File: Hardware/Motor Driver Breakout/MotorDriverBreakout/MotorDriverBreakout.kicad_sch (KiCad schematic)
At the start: 49 parts, among them U1 DRV8234RTER, U2 DRV8234RTER, U2 MCP4725A1T-E/CH, U3 MCP4725A1T-E/CH, U5 TPSM33625RDNR, U7 TPSM33625RDNR, U8 TPSM33625RDNR

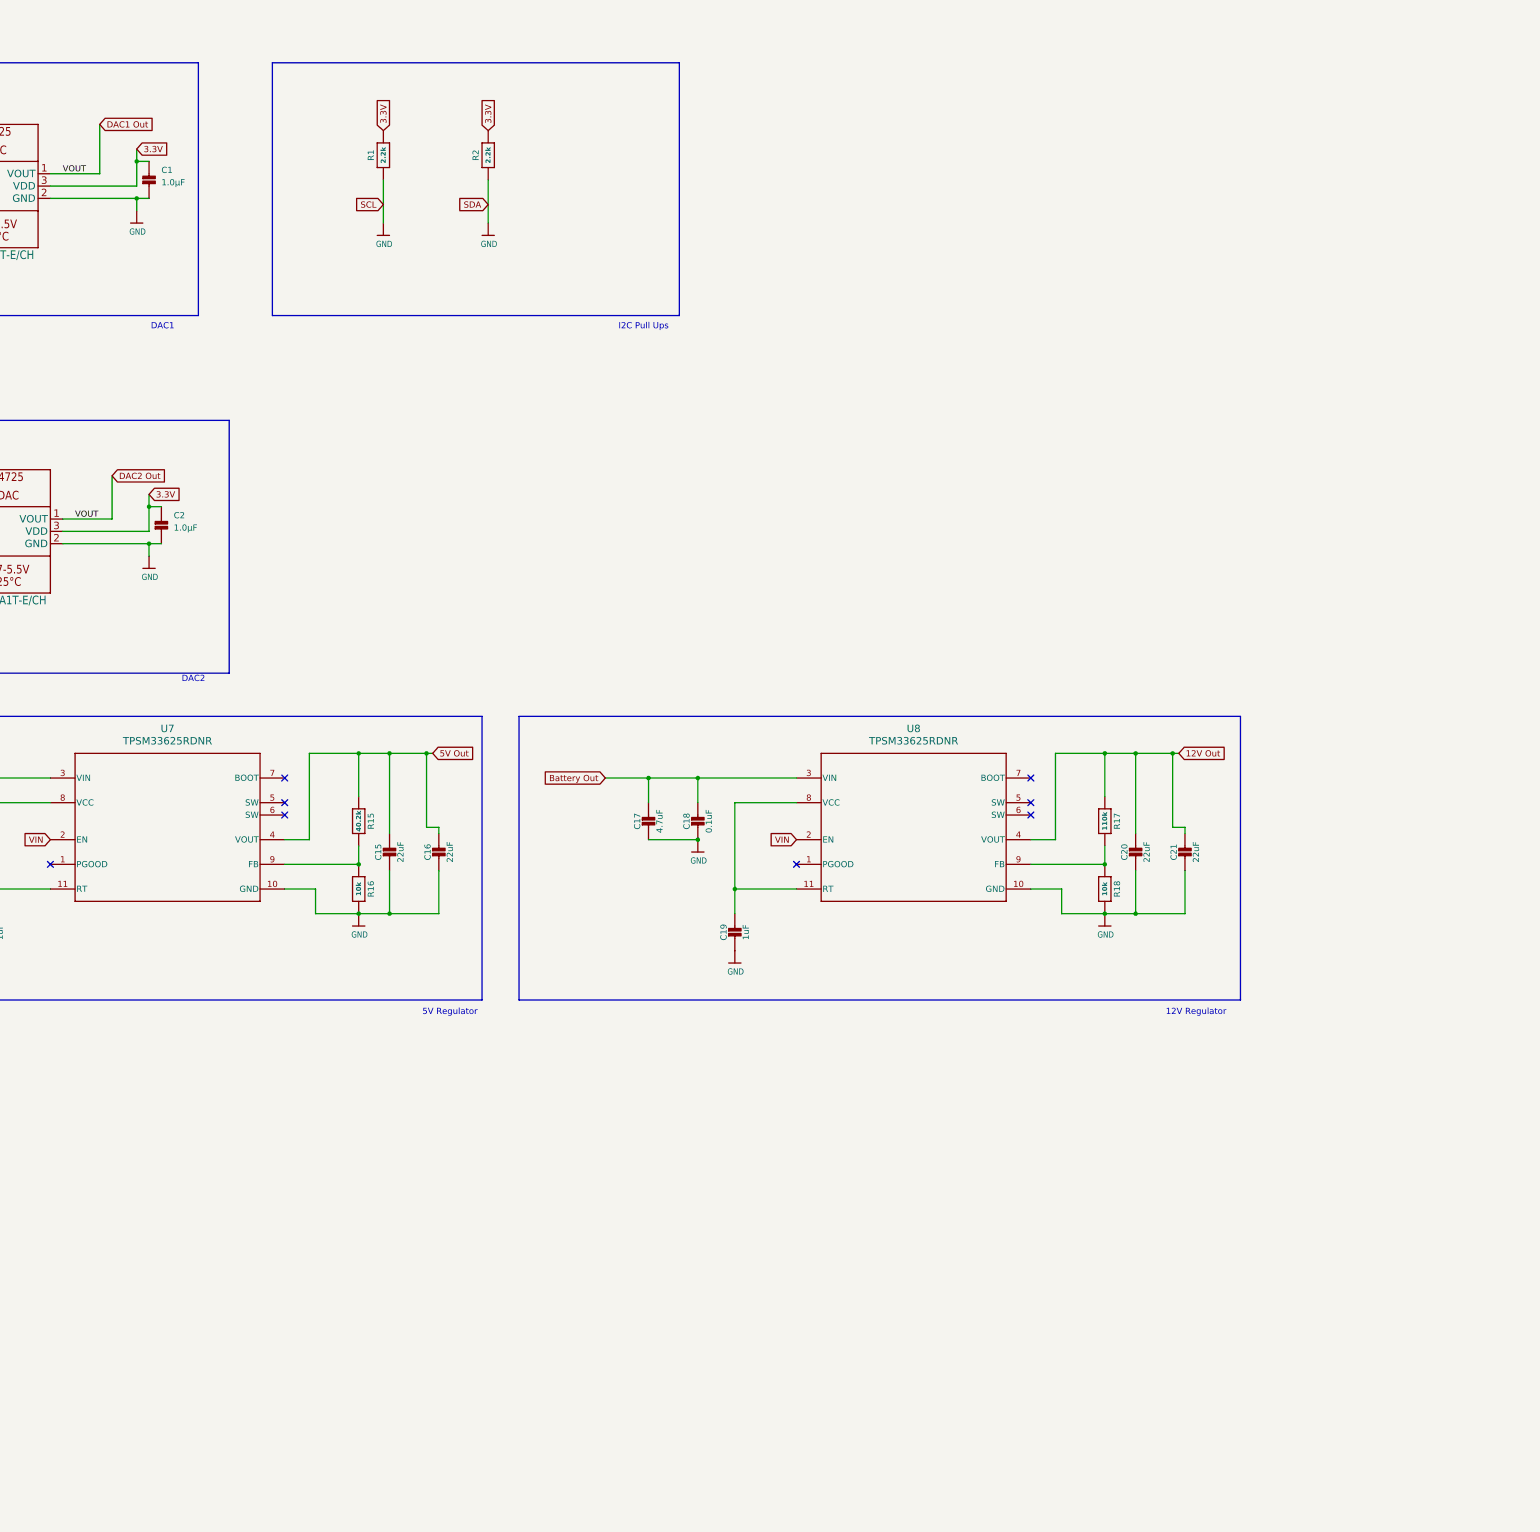
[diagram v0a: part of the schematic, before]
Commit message: Added another driver
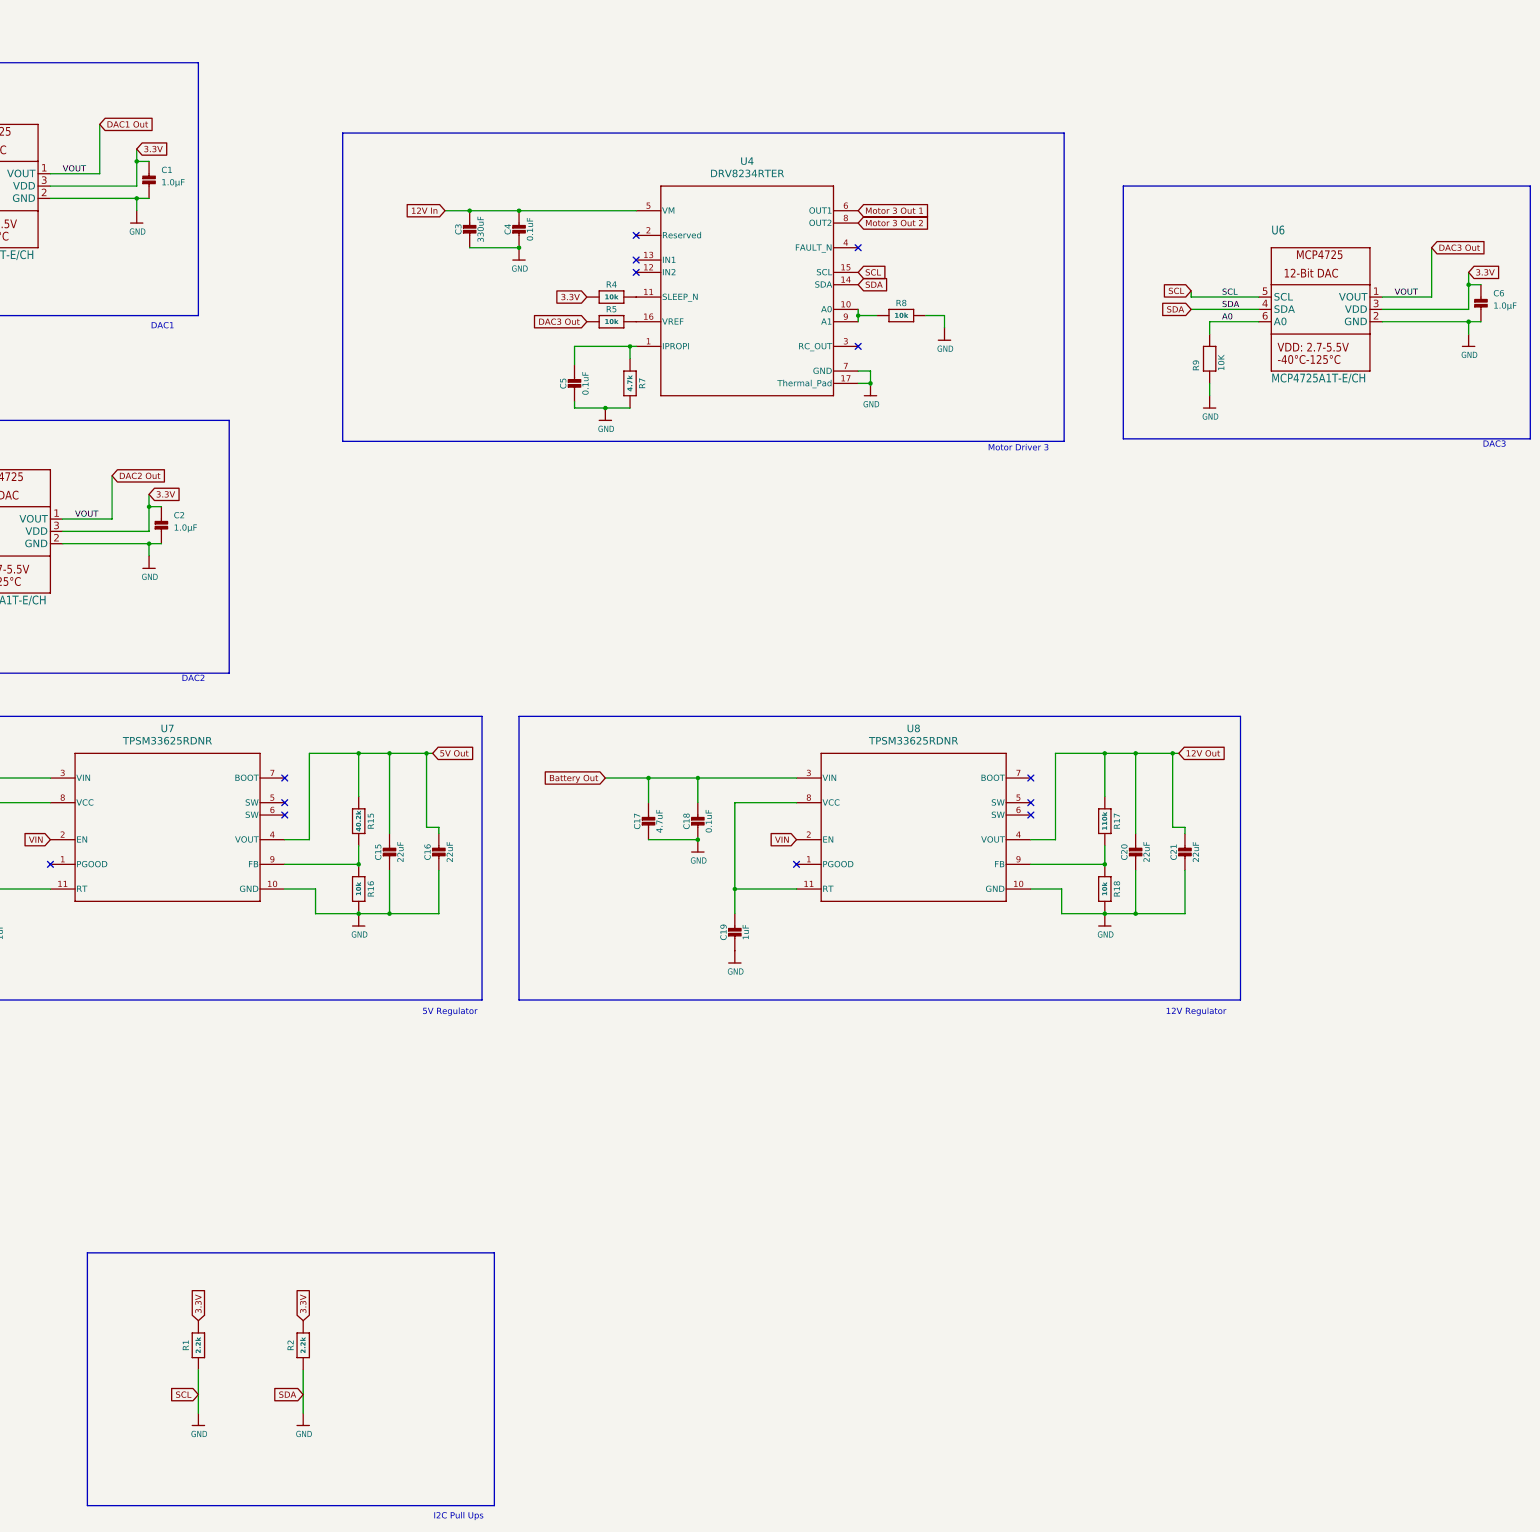
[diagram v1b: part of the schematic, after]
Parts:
- added C3: 330uF, Adafruit MPM3610:0805-NO, symbol Adafruit MPM3610-eagle-import:CAP_CERAMIC0805-NOOUTLINE
- added C4, C5: 0.1uF, Adafruit MPM3610:0805-NO, symbol Adafruit MPM3610-eagle-import:CAP_CERAMIC0805-NOOUTLINE
- added C6: 1.0µF, Adafruit MCP4725 Original:0805, symbol Adafruit MCP4725 Original-eagle-import:CAP_CERAMIC0805
- added R4, R5, R8: 10k, Adafruit MPM3610:0603-NO, symbol Adafruit MPM3610-eagle-import:RESISTOR_0603_NOOUT
- added R7: 4.7k, Adafruit MPM3610:0603-NO, symbol Adafruit MPM3610-eagle-import:RESISTOR_0603_NOOUT
- added R9: 10K, Adafruit MCP4725 Original:0805, symbol Adafruit MCP4725 Original-eagle-import:RESISTOR0805
- added U4: DRV8234RTER, RTE0016C-IPC_A, symbol 2025-12-19_19-45-19:DRV8234RTER
- added U6: MCP4725A1T-E/CH, Adafruit MCP4725 Original:SOT23-6, symbol Adafruit MCP4725 Original-eagle-import:DAC_MCP4725
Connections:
- net 12V In: now also C3.1, C4.1, U4.5 (VM)
- net 3.3V: now also C6.1 (P$1), R4.1, U6.3 (VDD)
- net A0: now also R9.2, U6.6 (A0)
- net DAC1 Out: now also R5.1, U6.1 (VOUT)
- net GND: now also C3.2, C4.2, C5.2, C6.2 (P$2), R7.2, R8.2, R9.1, U4.14 (SDA), U4.15 (SCL), U4.17 (Thermal_Pad), U4.7 (GND), U6.2 (GND), U6.4 (SDA), U6.5 (SCL)
- new net: R5.2, U4.16 (VREF)
- new net: R4.2, U4.11 (SLEEP_N)
- new net: R8.1, U4.10 (A0), U4.9 (A1)
- new net: C5.1, R7.1, U4.1 (IPROPI)
- new net Motor 3 Out 1: U4.6 (OUT1)
- new net Motor 3 Out 2: U4.8 (OUT2)
- no-connect marks 22 -> 27
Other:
- note added: "DAC3"
- note added: "Motor Driver 3"
- moved on the sheet: R1, R2

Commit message: Added voltage and current monitoring
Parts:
- added C28: 0.1µF, Adafruit_INA219_CurPowerMonitor:0805, symbol Adafruit_INA219_CurPowerMonitor-eagle-import:CAP_CERAMIC0805
- added R10, R11: 10K, Adafruit_INA219_CurPowerMonitor:0805, symbol Adafruit_INA219_CurPowerMonitor-eagle-import:RESISTOR0805
- added R12: 0.05, 0.1%, Adafruit_INA219_CurPowerMonitor:2512, symbol Adafruit_INA219_CurPowerMonitor-eagle-import:RESISTOR2512
- added U9: INA219BIDCNT, Adafruit_INA219_CurPowerMonitor:SOT23-8, symbol Adafruit_INA219_CurPowerMonitor-eagle-import:INA219
- U6: value MCP4725A1T-E/CH -> MCP4725A2T-E/CH
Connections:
- net 3.3V: now also R6.1
- net GND: now also C28.2 (P$2), R10.1, R11.1, U9.3 (GND), U9.5 (SCL), U9.6 (SDA); no longer R6.1
- new net: R10.2, U9.7 (A0)
- new net: R11.2, U9.8 (A1)
- new net Battery In: R12.2, U9.1 (VIN+)
- new net VCC: C28.1 (P$1), U9.4 (VCC)
- new net Voltage Out: R12.1, U9.2 (VIN-)
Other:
- note added: "Voltage/Current Monitor"
- moved on the sheet: R1, R2

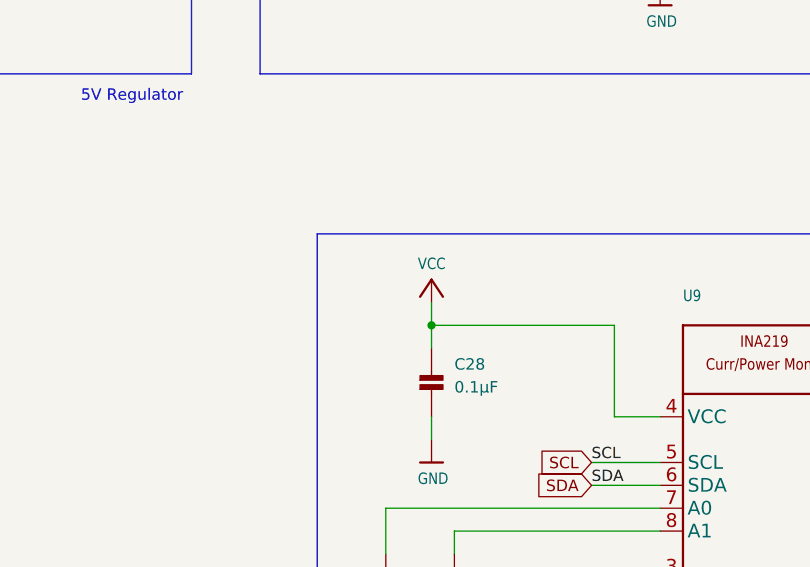
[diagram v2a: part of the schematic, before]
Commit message: Updated base station code to work with tip motors
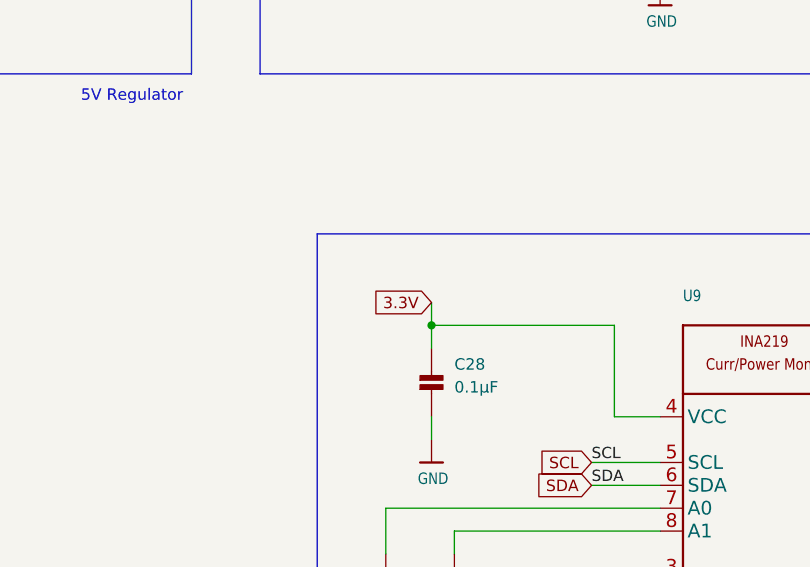
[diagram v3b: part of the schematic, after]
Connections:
- net VCC is gone; now on net 3.3V: C28.1 (P$1), U9.4 (VCC)
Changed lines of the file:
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@@
+	(global_label "3.3V"
+		(shape input)
+		(at 358.14 259.08 180)
+		(fields_autoplaced yes)
+		(effects
+			(font
+				(size 1.27 1.27)
+			)
+			(justify right)
+		)
+		(property "Intersheetrefs" "${INTERSHEET_REFS}"
+			(at 351.0424 259.08 0)
+			(effects
+				(font
+					(size 1.27 1.27)
+				)
+				(justify right)
+				(hide yes)
+			)
+		)
+	)
 	(global_label "3.3V"
 		(shape input)
@@
 					(unit 1)
 				)
-			)
-		)
-	)
-	(symbol
-		(lib_id "Adafruit_INA219_CurPowerMonitor-eagle-import:VCC")
-		(at 358.14 259.08 0)
-		(unit 1)
-		(exclude_from_sim no)
-		(in_bom yes)
-		(on_board yes)
-		(dnp no)
-		(property "Reference" "#P+3"
-			(at 358.14 259.08 0)
-			(effects
-				(font
-					(size 1.27 1.27)
-				)
-				(hide yes)
-			)
-		)
-		(property "Value" "VCC"
-			(at 356.616 255.524 0)
-			(effects
-				(font
-					(size 1.27 1.0795)
-				)
-				(justify left bottom)
-			)
-		)
-		(property "Footprint" ""
-			(at 358.14 259.08 0)
-			(effects
-				(font
-					(size 1.27 1.27)
-				)
-				(hide yes)
-			)
-		)
-		(property "Datasheet" ""
-			(at 358.14 259.08 0)
-			(effects
-				(font
-					(size 1.27 1.27)
-				)
-				(hide yes)
-			)
-		)
-		(property "Description" ""
-			(at 358.14 259.08 0)
-			(effects
-				(font
-					(size 1.27 1.27)
-				)
-				(hide yes)
-			)
-		)
-		(pin "1"
-		)
-		(instances
-			(project "MotorDriverBreakout"
-				(path "/8c7fbb5f-9bb2-4d3a-9fa8-9df6e610b209"
-					(reference "#P+3")
-					(unit 1)
-				)
